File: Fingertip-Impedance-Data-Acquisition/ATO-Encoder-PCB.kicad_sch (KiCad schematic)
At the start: 28 parts, among them IC1 MCP2561-H_P, J1 DE9_Socket, J2 B2B-XH-A, J3 B2B-XH-A, J4 Conn_01x06, J5 Screw_Terminal_01x02

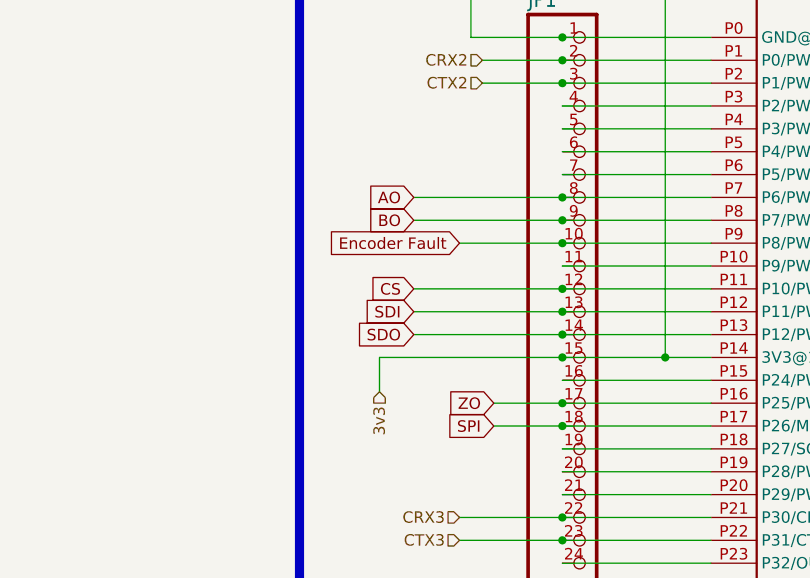
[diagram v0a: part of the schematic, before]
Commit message: Updated design to be compatible with quadrature decoding without CPU intervention. OSH Park order was updated
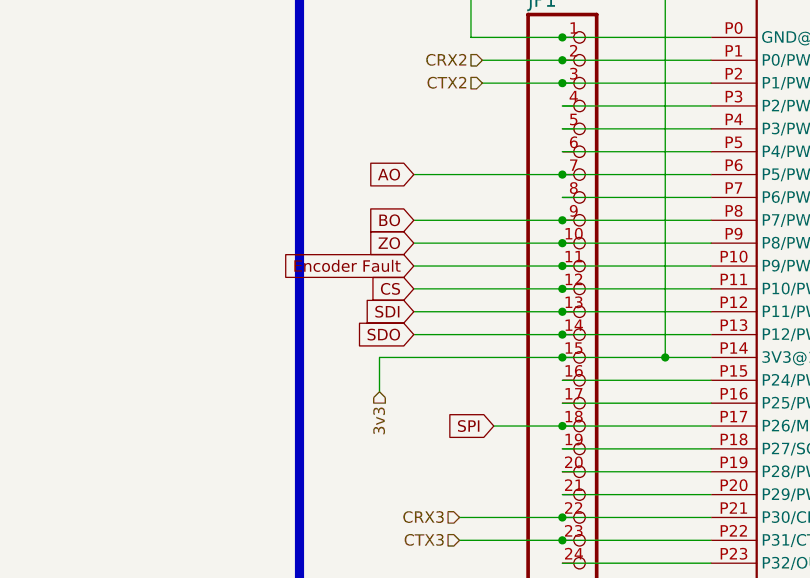
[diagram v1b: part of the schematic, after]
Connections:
- net AO: now also JP1.7, U$1.P6 (P5/PWM/IN2); no longer JP1.8, U$1.P7 (P6/PWM/OUT1D)
- net Encoder Fault: now also JP1.11, U$1.P10 (P9/PWM/OUT1C); no longer JP1.10, U$1.P9 (P8/PWM/IN1/TX2)
- net ZO: now also JP1.10, U$1.P9 (P8/PWM/IN1/TX2); no longer JP1.17, U$1.P16 (P25/PWM/SDA2/RX6/A11)
- new net: JP1.17, U$1.P16 (P25/PWM/SDA2/RX6/A11)
- new net: JP1.8, U$1.P7 (P6/PWM/OUT1D)
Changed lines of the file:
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@@
+	)
+	(junction
+		(at 322.58 74.93)
+		(diameter 0)
+		(color 0 0 0 0)
+	)
+	(junction
+		(at 204.47 110.49)
+		(diameter 0)
+		(color 0 0 0 0)
+	)
+	(junction
+		(at 204.47 62.23)
+		(diameter 0)
+		(color 0 0 0 0)
+	)
+	(junction
+		(at 49.53 222.25)
+		(diameter 0)
+		(color 0 0 0 0)
+	)
+	(junction
+		(at 314.96 57.15)
+		(diameter 0)
+		(color 0 0 0 0)
+	)
+	(junction
+		(at 66.04 64.77)
+		(diameter 0)
+		(color 0 0 0 0)
+	)
+	(junction
+		(at 322.58 62.23)
+		(diameter 0)
+		(color 0 0 0 0)
+	)
+	(junction
+		(at 63.5 67.31)
+		(diameter 0)
+		(color 0 0 0 0)
+	)
+	(junction
+		(at 74.93 45.72)
+		(diameter 0)
+		(color 0 0 0 0)
+	)
+	(junction
+		(at 317.5 59.69)
+		(diameter 0)
+		(color 0 0 0 0)
+	)
+	(junction
+		(at 322.58 57.15)
+		(diameter 0)
+		(color 0 0 0 0)
+	)
+	(junction
+		(at 204.47 100.33)
+		(diameter 0)
+		(color 0 0 0 0)
+	)
+	(junction
+		(at 322.58 92.71)
+		(diameter 0)
+		(color 0 0 0 0)
 	)
 	(junction
@@
 	)
 	(junction
-		(at 322.58 74.93)
-		(diameter 0)
-		(color 0 0 0 0)
-	)
-	(junction
-		(at 204.47 110.49)
-		(diameter 0)
-		(color 0 0 0 0)
-	)
-	(junction
-		(at 204.47 62.23)
-		(diameter 0)
-		(color 0 0 0 0)
-	)
-	(junction
-		(at 49.53 222.25)
-		(diameter 0)
-		(color 0 0 0 0)
-	)
-	(junction
-		(at 314.96 57.15)
-		(diameter 0)
-		(color 0 0 0 0)
-	)
-	(junction
-		(at 66.04 64.77)
-		(diameter 0)
-		(color 0 0 0 0)
-	)
-	(junction
-		(at 322.58 62.23)
-		(diameter 0)
-		(color 0 0 0 0)
-	)
-	(junction
-		(at 63.5 67.31)
-		(diameter 0)
-		(color 0 0 0 0)
-	)
-	(junction
-		(at 74.93 45.72)
-		(diameter 0)
-		(color 0 0 0 0)
-	)
-	(junction
-		(at 317.5 59.69)
-		(diameter 0)
-		(color 0 0 0 0)
-	)
-	(junction
-		(at 322.58 57.15)
-		(diameter 0)
-		(color 0 0 0 0)
-	)
-	(junction
-		(at 204.47 100.33)
-		(diameter 0)
-		(color 0 0 0 0)
-	)
-	(junction
-		(at 204.47 74.93)
-		(diameter 0)
-		(color 0 0 0 0)
-	)
-	(junction
-		(at 322.58 92.71)
+		(at 204.47 72.39)
 		(diameter 0)
 		(color 0 0 0 0)
@@
 	)
 	(junction
+		(at 204.47 82.55)
+		(diameter 0)
+		(color 0 0 0 0)
+	)
+	(junction
 		(at 58.42 72.39)
 		(diameter 0)
@@
 	)
 	(junction
-		(at 204.47 97.79)
-		(diameter 0)
-		(color 0 0 0 0)
-	)
-	(junction
 		(at 204.47 92.71)
 		(diameter 0)
@@
 		(diameter 0)
 		(color 0 0 0 0)
-	)
-	(wire
-		(pts
-			(xy 193.04 80.01) (xy 204.47 80.01)
-		)
-		(stroke
-			(width 0)
-			(type default)
-		)
 	)
 	(wire
@@
 	(wire
 		(pts
+			(xy 187.96 82.55) (xy 204.47 82.55)
+		)
+		(stroke
+			(width 0)
+			(type default)
+		)
+	)
+	(wire
+		(pts
 			(xy 109.22 121.92) (xy 109.22 124.46)
 		)
@@
 	(wire
 		(pts
+			(xy 187.96 72.39) (xy 204.47 72.39)
+		)
+		(stroke
+			(width 0)
+			(type default)
+		)
+	)
+	(wire
+		(pts
 			(xy 219.71 191.77) (xy 219.71 181.61)
 		)
@@
 	(wire
 		(pts
-			(xy 196.85 97.79) (xy 204.47 97.79)
-		)
-		(stroke
-			(width 0)
-			(type default)
-		)
-	)
-	(wire
-		(pts
 			(xy 317.5 44.45) (xy 317.5 59.69)
 		)
@@
 	(wire
 		(pts
+			(xy 187.96 80.01) (xy 204.47 80.01)
+		)
+		(stroke
+			(width 0)
+			(type default)
+		)
+	)
+	(wire
+		(pts
 			(xy 304.8 113.03) (xy 322.58 113.03)
 		)
@@
 		(pts
 			(xy 58.42 213.36) (xy 58.42 214.63)
-		)
-		(stroke
-			(width 0)
-			(type default)
-		)
-	)
-	(wire
-		(pts
-			(xy 187.96 74.93) (xy 204.47 74.93)
 		)
 		(stroke
@@
 	(global_label "AO"
 		(shape input)
-		(at 187.96 74.93 180)
+		(at 187.96 72.39 180)
 		(fields_autoplaced yes)
 		(effects
@@
 		)
 		(property "Intersheetrefs" "${INTERSHEET_REFS}"
-			(at 182.5557 74.93 0)
+			(at 182.5557 72.39 0)
 			(effects
 				(font
@@
 	(global_label "Encoder Fault"
 		(shape input)
-		(at 193.04 80.01 180)
+		(at 187.96 82.55 180)
 		(fields_autoplaced yes)
 		(effects
@@
 		)
 		(property "Intersheetrefs" "${INTERSHEET_REFS}"
-			(at 176.7503 80.01 0)
+			(at 171.6703 82.55 0)
 			(effects
 				(font
@@
 	(global_label "ZO"
 		(shape input)
-		(at 196.85 97.79 180)
+		(at 187.96 80.01 180)
 		(fields_autoplaced yes)
 		(effects
@@
 		)
 		(property "Intersheetrefs" "${INTERSHEET_REFS}"
-			(at 191.3248 97.79 0)
+			(at 182.4348 80.01 0)
 			(effects
 				(font

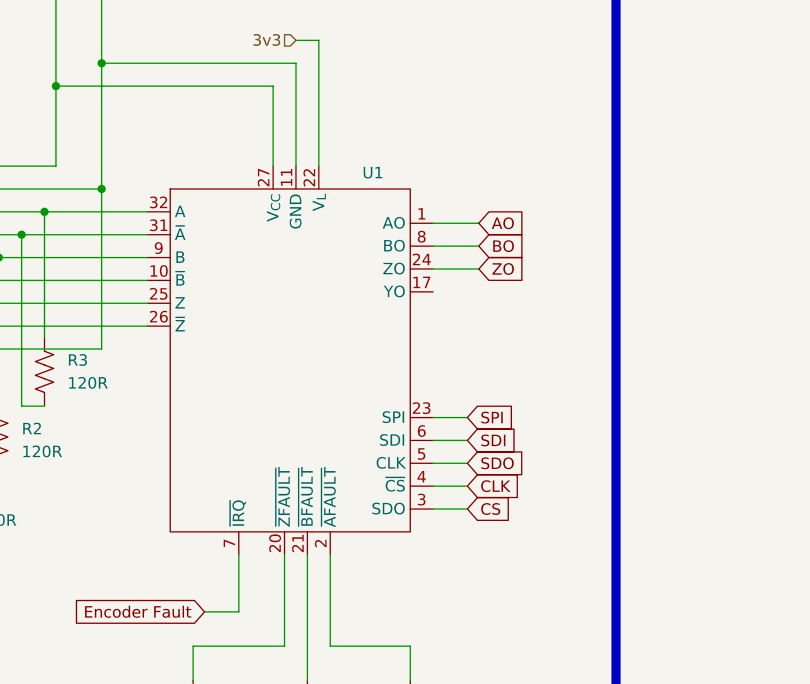
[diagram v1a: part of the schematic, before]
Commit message: Fixed SPI inteface to MAX chip
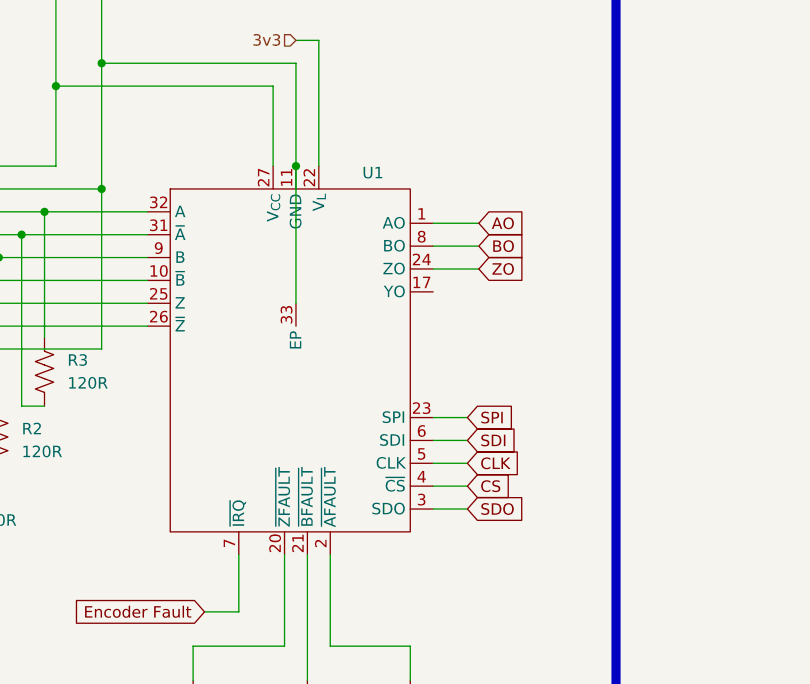
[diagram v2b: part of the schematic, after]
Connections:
- net CLK: now also U1.5 (CLK); no longer U1.4 (~{CS})
- net CS: now also U1.4 (~{CS}); no longer U1.3 (SDO)
- net GND: now also U1.33 (EP)
- net SDO: now also U1.3 (SDO); no longer U1.5 (CLK)
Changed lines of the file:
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@@
 	)
 	(junction
+		(at 96.52 57.15)
+		(diameter 0)
+		(color 0 0 0 0)
+	)
+	(junction
 		(at 204.47 90.17)
 		(diameter 0)
@@
 	(wire
 		(pts
+			(xy 96.52 57.15) (xy 96.52 72.39)
+		)
+		(stroke
+			(width 0)
+			(type default)
+		)
+	)
+	(wire
+		(pts
 			(xy 53.34 67.31) (xy 63.5 67.31)
 		)
@@
 		)
 	)
-	(global_label "SDO"
+	(global_label "CLK"
 		(shape input)
 		(at 115.57 90.17 0)
@@
 		)
 		(property "Intersheetrefs" "${INTERSHEET_REFS}"
-			(at 122.3652 90.17 0)
+			(at 122.1233 90.17 0)
 			(effects
 				(font
@@
 		)
 	)
-	(global_label "CLK"
+	(global_label "CS"
 		(shape input)
 		(at 115.57 92.71 0)
@@
 		)
 		(property "Intersheetrefs" "${INTERSHEET_REFS}"
-			(at 122.1233 92.71 0)
+			(at 121.0347 92.71 0)
 			(effects
 				(font
@@
 		)
 	)
-	(global_label "CS"
+	(global_label "SDO"
 		(shape input)
 		(at 115.57 95.25 0)
@@
 		)
 		(property "Intersheetrefs" "${INTERSHEET_REFS}"
-			(at 121.0347 95.25 0)
+			(at 122.3652 95.25 0)
 			(effects
 				(font
@@
 		(pin "3"
 		)
+		(pin "33"
+		)
 		(instances
